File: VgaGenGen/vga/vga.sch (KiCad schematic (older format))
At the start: 3 parts

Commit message: added VGA ROM image and schematic
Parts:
- removed U?: 74LS161, symbol 74xx:74LS161
- added U?: 27C512, Package_DIP:DIP-28_W15.24mm, symbol Memory_EPROM:27C512
- added X?: CXO_DIP14, Oscillator:Oscillator_DIP-14, symbol Oscillator:CXO_DIP14
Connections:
- net labels added: Blanking, GND, Video, h0, h1, h2, h3, h4, h5, hSync, v0, v1, v2, v3, v4, v5, v6, v7, v8, v9, vSync
- wire segments 0 -> 48
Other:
- moved on the sheet: U?

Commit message: working on the calculator and the A32 pcb
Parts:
- added C?: C, symbol Device:C
- added R?: R, symbol Device:R
- added U?: 74LS165, symbol 74xx:74LS165
- added U? (x4): 74LS14, symbol 74xx:74LS14
- added U? (x4): 74LS08, symbol 74xx:74LS08
- gave numbers to parts that had none: 1
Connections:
- net labels added: A11, A12, A13, A14, A15, TestScreenVideo, VRAMSEL, VRAMSEL'
- net labels removed: Video
- wire segments 48 -> 90
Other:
- moved on the sheet: U?, X25.175MHz

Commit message: updated the VGA schematic with a shift register
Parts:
- added U?: 28C256, symbol Memory_EEPROM:28C256
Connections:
- net labels added: +5V, PixelClock, Px0, Px1, Px2, Video
- wire segments 90 -> 112
- no-connect marks 0 -> 7

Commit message: adding font handling programs and fonts.
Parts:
- removed U? (x3): 74LS14, symbol 74xx:74LS14
- removed U? (x4): 74LS08, symbol 74xx:74LS08
- removed U?: 28C256, symbol Memory_EEPROM:28C256
- added CharROM: 27C256, Package_DIP:DIP-28_W15.24mm, symbol Memory_EPROM:27C256
- added VRAM: IDT7132, symbol Memory_RAM:IDT7132
- C?: value C -> 18p
- R?: value R -> 1k
- gave numbers to parts that had none: 3
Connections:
- net labels added: A0, A1, A10, A2, A3, A4, A5, A6, A7, A8, A9, D0, D1, D2, D3, D4, D5, D6, D7, NMI, RD, WAIT, WR, asc0, asc1, asc2, asc3, asc4, asc5, asc6, asc7, ch0, ch1, ch2, ch3, ch4, ch5, ch6, ch7
- net labels removed: A11, A12, A13, A14, A15, Px0, Px1, Px2, VRAMSEL'
- wire segments 112 -> 130
- no-connect marks 7 -> 9
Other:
- moved on the sheet: C?, R?, U?, U?D

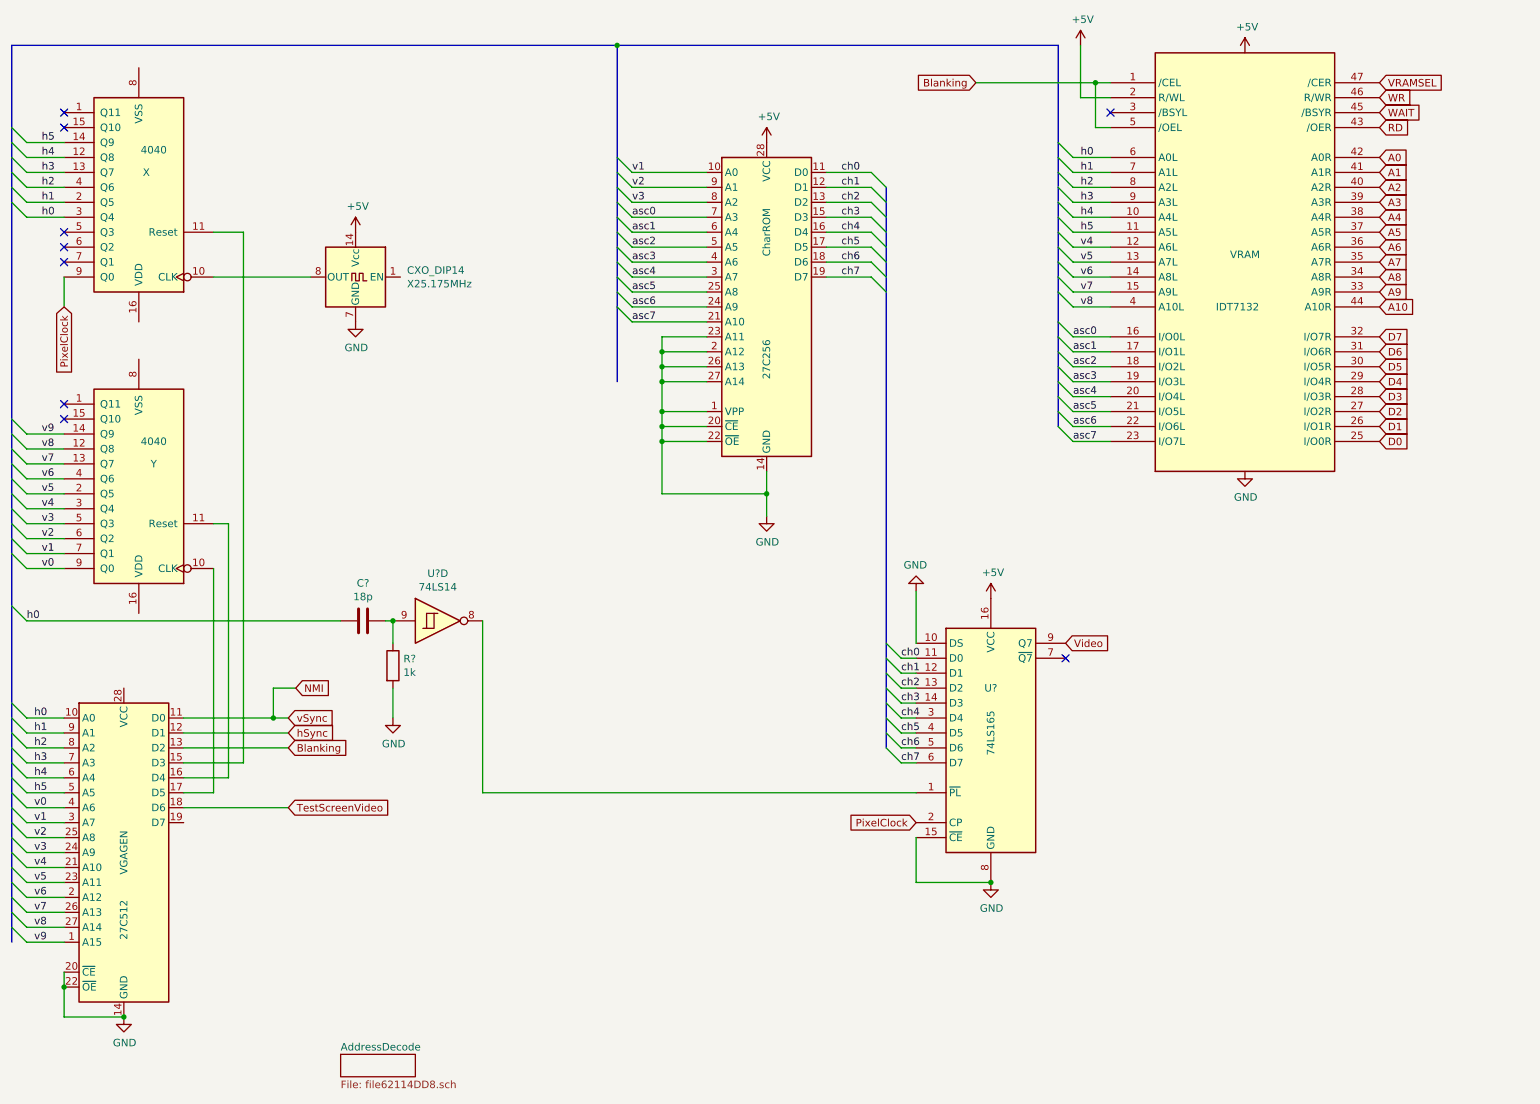
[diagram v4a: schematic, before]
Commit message: Doc changes
Removed a '32 from A32
Documented the VGA connector
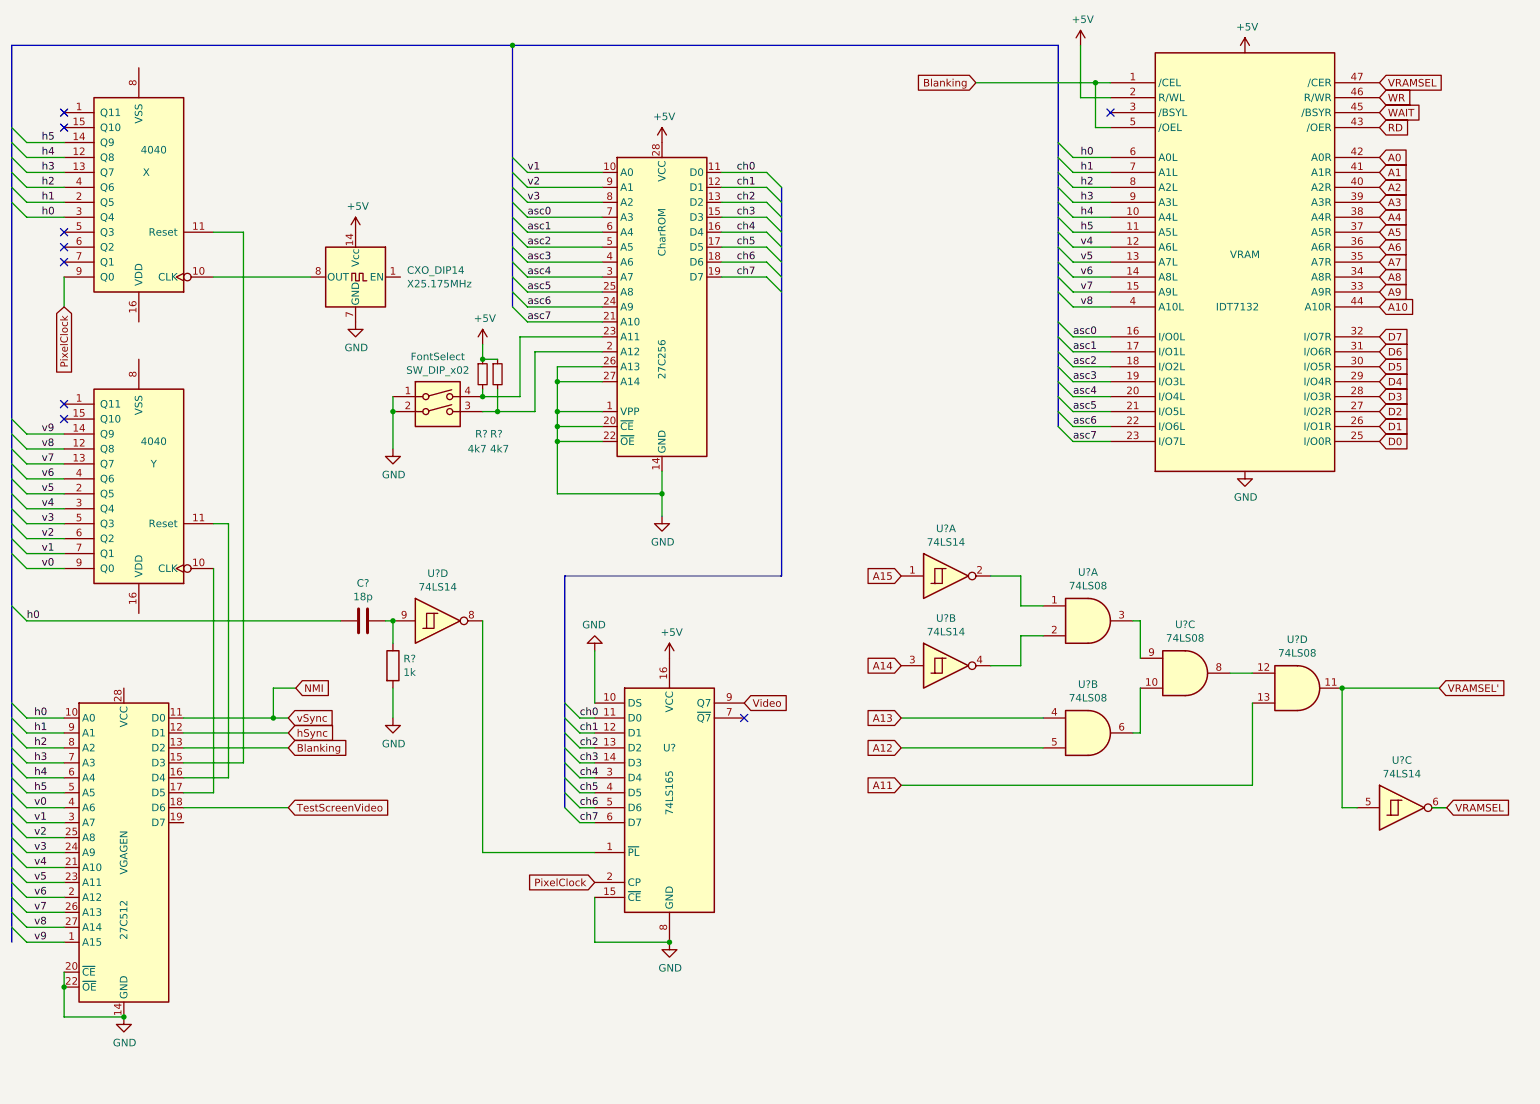
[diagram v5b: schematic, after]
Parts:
- added FontSelect: SW_DIP_x02, symbol Switch:SW_DIP_x02
- added R? (x2): 4k7, symbol Device:R_Small
- added U? (x3): 74LS14, symbol 74xx:74LS14
- added U? (x4): 74LS08, symbol 74xx:74LS08
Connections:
- net +5V: now also R?.1, R?.1
- net GND: now also FontSelect.1, FontSelect.2; no longer CharROM.2 (A12), CharROM.23 (A11)
- net VRAMSEL: now also U?.6
- new net: U?.1, U?.2
- new net: U?.2, U?.4
- new net: U?.3, U?.9
- new net: U?.10, U?.6
- new net: U?.12, U?.8
- new net: CharROM.2 (A12), FontSelect.3, R?.2
- new net: CharROM.23 (A11), FontSelect.4, R?.2
- new net A11: U?.13
- new net A12: U?.5
- new net A13: U?.4
- new net A14: U?.3
- new net A15: U?.1
- new net VRAMSEL': U?.11, U?.5
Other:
- moved on the sheet: CharROM, U?

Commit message: updated schematics, memory bank switching code and memory map documentation
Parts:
- added D?: D_Schottky, symbol Device:D_Schottky
- added R?: R_Small, symbol Device:R_Small
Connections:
- net +5V: now also R?.1
- net VRAMSEL: now also R?.2
- net WAIT: now also D?.2 (A); no longer VRAM.45 (/BSYR)
- new net: D?.1 (K), VRAM.45 (/BSYR)
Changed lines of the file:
@@
 Wire Wire Line
 	1050 4550 3150 4550
-Text GLabel 10100 1150 2    50   Input ~ 0
+Text GLabel 10750 1150 2    50   Input ~ 0
 WAIT
 Text GLabel 7400 950  0    50   Input ~ 0
 Blanking
-Text GLabel 10100 950  2    50   Input ~ 0
+Text GLabel 10600 950  2    50   Input ~ 0
 VRAMSEL
 Text GLabel 10100 1450 2    50   Input ~ 0
@@
 Wire Wire Line
 	4100 2700 4100 2800
+Connection ~ 4100 2800
+$Comp
+L power:+5V #PWR?
+U 1 1 622602D6
+P 10900 700
+F 0 "#PWR?" H 10900 550 50  0001 C CNN
+F 1 "+5V" H 10915 873 50  0000 C CNN
+F 2 "" H 10900 700 50  0001 C CNN
+F 3 "" H 10900 700 50  0001 C CNN
+	1    10900 700
+	1    0    0    -1
+$EndComp
+$Comp
+L Device:R_Small R?
+U 1 1 62260EEC
+P 10450 800
+F 0 "R?" V 10254 800 50  0000 C CNN
+F 1 "R_Small" V 10345 800 50  0000 C CNN
+F 2 "" H 10450 800 50  0001 C CNN
+F 3 "~" H 10450 800 50  0001 C CNN
+	1    10450 800
+	0    1    1    0
+$EndComp
+Connection ~ 10100 950
+$Comp
+L Device:D_Schottky D?
+U 1 1 6227D84D
+P 10450 1150
+F 0 "D?" H 10600 1200 50  0000 C CNN
+F 1 "D_Schottky" H 10550 1050 50  0000 C CNN
+F 2 "" H 10450 1150 50  0001 C CNN
+F 3 "~" H 10450 1150 50  0001 C CNN
+	1    10450 1150
+	1    0    0    -1
+$EndComp
+Wire Wire Line
+	10600 1150 10750 1150
+Wire Wire Line
+	10300 1150 10100 1150
+Wire Wire Line
+	10100 950  10600 950
+Wire Wire Line
+	10350 800  10100 800
+Wire Wire Line
+	10100 800  10100 950
+Wire Wire Line
+	10550 800  10900 800
+Wire Wire Line
+	10900 800  10900 700
 Wire Bus Line
 	6100 1650 6100 4250
@@
 Wire Bus Line
 	950  700  950  6700
-Connection ~ 4100 2800
 $EndSCHEMATC
